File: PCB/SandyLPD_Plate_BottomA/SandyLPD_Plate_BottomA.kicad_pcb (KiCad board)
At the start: 2 copper layers, 131 x 83 mm, 14 parts

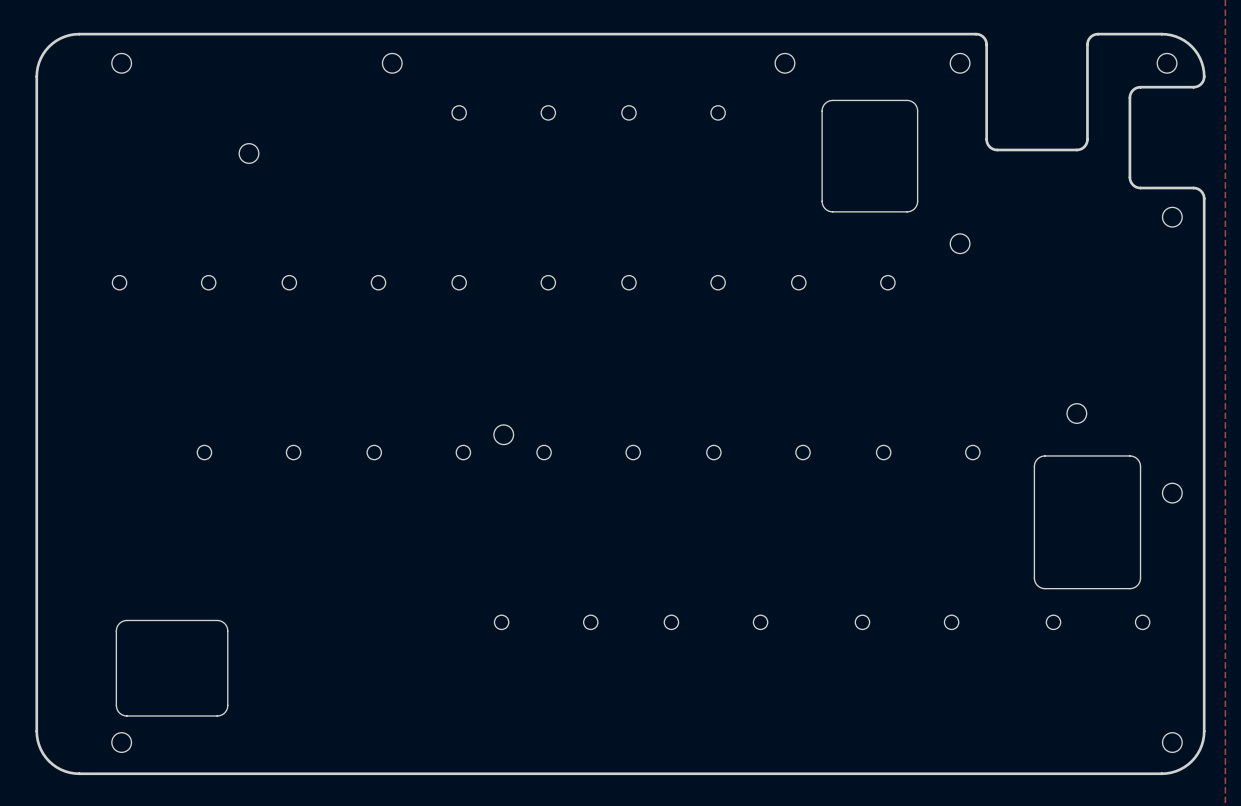
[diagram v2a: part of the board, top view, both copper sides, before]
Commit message: ネジ穴位置を再調整。
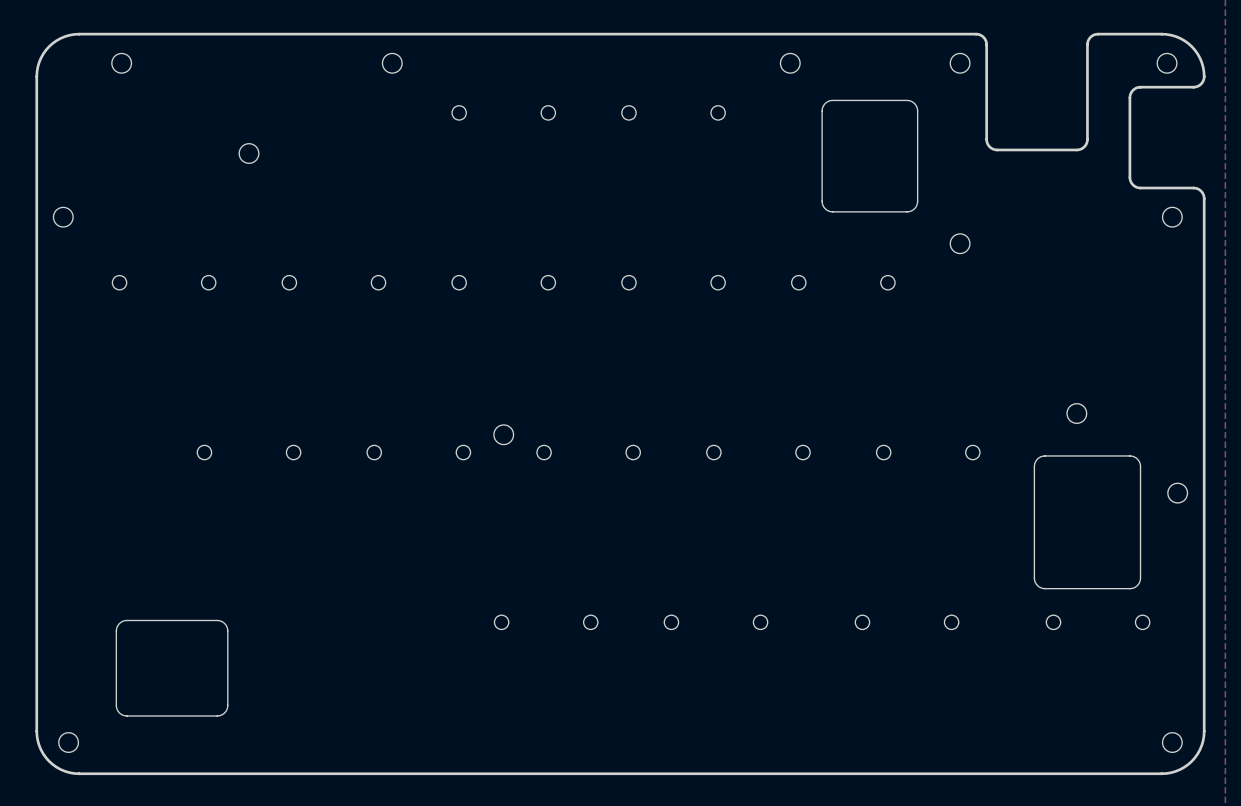
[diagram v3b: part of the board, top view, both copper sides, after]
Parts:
- added H_mid_8: MountingHole, locallib:MountingHole_2.2mm_M2_no_REF, F.Cu at (26.4, 52.6)
- moved H_btm_3 5.95 mm to (27.0, 111.5)
- moved H_mid_3 0.60 mm to (108.0, 35.3)
- moved H_mid_17 0.60 mm to (151.4, 83.6)
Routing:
- added copper zone on B.Cu, net (none)
- added copper zone on F.Cu, net (none)
- removed copper zone on B.Cu, net GND
- removed copper zone on F.Cu, net GND
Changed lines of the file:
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@@
 	)
 	(net 0 "")
-	(net 1 "GND")
 	(footprint "locallib:MountingHole_2.2mm_M2_no_REF"
 		(layer "F.Cu")
@@
 	(footprint "locallib:MountingHole_2.2mm_M2_no_REF"
 		(layer "F.Cu")
-		(at 150.836667 83.558138 180)
+		(at 151.431976 83.558138 180)
 		(descr "Mounting Hole 2.2mm, no annular, M2")
 		(tags "mounting hole 2.2mm no annular m2")
@@
 	(footprint "locallib:MountingHole_2.2mm_M2_no_REF"
 		(layer "F.Cu")
-		(at 107.378818 35.337425)
+		(at 107.974127 35.337425)
 		(descr "Mounting Hole 2.2mm, no annular, M2")
 		(tags "mounting hole 2.2mm no annular m2")
@@
 	(footprint "locallib:MountingHole_2.2mm_M2_no_REF"
 		(layer "F.Cu")
+		(at 26.416246 52.601856)
+		(descr "Mounting Hole 2.2mm, no annular, M2")
+		(tags "mounting hole 2.2mm no annular m2")
+		(property "Reference" "H_mid_8"
+			(at 0 -3.2 0)
+			(layer "F.SilkS")
+			(hide yes)
+			(effects
+				(font
+					(size 1 1)
+					(thickness 0.15)
+				)
+			)
+		)
+		(property "Value" "MountingHole"
+			(at 0 3.2 0)
+			(layer "F.Fab")
+			(effects
+				(font
+					(size 1 1)
+					(thickness 0.15)
+				)
+			)
+		)
+		(property "Footprint" "locallib:MountingHole_2.2mm_M2_no_REF"
+			(at 0 0 0)
+			(unlocked yes)
+			(layer "F.Fab")
+			(hide yes)
+			(effects
+				(font
+					(size 1.27 1.27)
+					(thickness 0.15)
+				)
+			)
+		)
+		(property "Datasheet" ""
+			(at 0 0 0)
+			(unlocked yes)
+			(layer "F.Fab")
+			(hide yes)
+			(effects
+				(font
+					(size 1.27 1.27)
+					(thickness 0.15)
+				)
+			)
+		)
+		(property "Description" "Mounting Hole without connection"
+			(at 0 0 0)
+			(unlocked yes)
+			(layer "F.Fab")
+			(hide yes)
+			(effects
+				(font
+					(size 1.27 1.27)
+					(thickness 0.15)
+				)
+			)
+		)
+		(property "LCSC-Reserve" ""
+			(at 0 0 0)
+			(unlocked yes)
+			(layer "F.Fab")
+			(hide yes)
+			(effects
+				(font
+					(size 1 1)
+					(thickness 0.15)
+				)
+			)
+		)
+		(property ki_fp_filters "MountingHole*")
+		(sheetname "ルート")
+		(sheetfile "SandyLPD_Plate_BottomA.kicad_sch")
+		(attr exclude_from_pos_files exclude_from_bom)
+		(fp_circle
+			(center 0 0)
+			(end 2.2 0)
+			(stroke
+				(width 0.15)
+				(type solid)
+			)
+			(fill none)
+			(layer "Cmts.User")
+		)
+		(fp_circle
+			(center 0 0)
+			(end 2.45 0)
+			(stroke
+				(width 0.05)
+				(type solid)
+			)
+			(fill none)
+			(layer "F.CrtYd")
+		)
+		(fp_text user "${REFERENCE}"
+			(at 0 0 0)
+			(layer "F.Fab")
+			(effects
+				(font
+					(size 1 1)
+					(thickness 0.15)
+				)
+			)
+		)
+		(pad "" np_thru_hole circle
+			(at 0 0)
+			(size 2.2 2.2)
+			(drill 2.2)
+			(layers "*.Cu" "*.Mask")
+		)
+	)
+	(footprint "locallib:MountingHole_2.2mm_M2_no_REF"
+		(layer "F.Cu")
 		(at 63.325656 35.337425)
 		(descr "Mounting Hole 2.2mm, no annular, M2")
@@
 	(footprint "locallib:MountingHole_2.2mm_M2_no_REF"
 		(layer "B.Cu")
-		(at 32.964693 111.537849 180)
+		(at 27.011559 111.537843 180)
 		(descr "Mounting Hole 2.2mm, no annular, M2")
 		(tags "mounting hole 2.2mm no annular m2")
@@
 	)
 	(zone
-		(net 1)
-		(net_name "GND")
+		(net 0)
+		(net_name "")
 		(layers "F&B.Cu")
 		(hatch edge 0.508)

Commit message: WIP　BaseにESDとヒューズ追加。ボトムAの穴位置調整中。
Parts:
- added C1: 10u, Capacitor_SMD:C_0805_2012Metric, B.Cu at (101.3, -48.5)
- added C10: 100n, Capacitor_SMD:C_0402_1005Metric, B.Cu at (129.4, -30.6)
- added C11: 100n, Capacitor_SMD:C_0402_1005Metric, B.Cu at (129.0, -34.8)
- added C12: 100n, Capacitor_SMD:C_0402_1005Metric, B.Cu at (125.8, -41.5)
- added C13: 2.2uF, Capacitor_SMD:C_0402_1005Metric, B.Cu at (125.8, -42.5)
- added C14: 2.2uF, Capacitor_SMD:C_0402_1005Metric, B.Cu at (121.6, -39.9)
- added C15: 2.2uF, Capacitor_SMD:C_0402_1005Metric, B.Cu at (120.6, -39.9)
- added C17: 10u, Capacitor_SMD:C_0805_2012Metric, B.Cu at (185.8, -48.3)
- added C18: 10u, Capacitor_SMD:C_0805_2012Metric, B.Cu at (185.8, -44.7)
- added C19: 100n, Capacitor_SMD:C_0402_1005Metric, B.Cu at (172.5, -22.9)
- added C2: 10u, Capacitor_SMD:C_0805_2012Metric, B.Cu at (101.3, -44.7)
- added C20: 100n, Capacitor_SMD:C_0402_1005Metric, B.Cu at (176.1, -37.6)
- added C21: 100n, Capacitor_SMD:C_0402_1005Metric, B.Cu at (181.3, -28.3)
- added C24: 100n, Capacitor_SMD:C_0402_1005Metric, B.Cu at (179.4, -32.5)
- added C28: 100n, Capacitor_SMD:C_0402_1005Metric, B.Cu at (173.5, -22.9)
- added C29: 100n, Capacitor_SMD:C_0402_1005Metric, B.Cu at (184.0, -41.1)
- added C3: 100n, Capacitor_SMD:C_0402_1005Metric, B.Cu at (125.7, -39.9)
- added C30: 100n, Capacitor_SMD:C_0402_1005Metric, B.Cu at (167.4, -28.4)
- added C31: 100n, Capacitor_SMD:C_0402_1005Metric, B.Cu at (175.1, -37.6)
- added C32: 100n, Capacitor_SMD:C_0402_1005Metric, B.Cu at (170.0, -37.6)
- added C33: 100n, Capacitor_SMD:C_0402_1005Metric, B.Cu at (168.4, -33.1)
- added C34: 2.2uF, Capacitor_SMD:C_0402_1005Metric, B.Cu at (185.2, -41.1)
- added C35: 2.2uF, Capacitor_SMD:C_0402_1005Metric, B.Cu at (172.0, -37.6)
- added C36: 2.2uF, Capacitor_SMD:C_0402_1005Metric, B.Cu at (171.0, -37.6)
- added C4: 100n, Capacitor_SMD:C_0402_1005Metric, B.Cu at (121.9, -25.4)
- added C5: 100n, Capacitor_SMD:C_0402_1005Metric, B.Cu at (124.7, -39.9)
- added C6: 100n, Capacitor_SMD:C_0402_1005Metric, B.Cu at (122.9, -25.4)
- added C7: 100n, Capacitor_SMD:C_0402_1005Metric, B.Cu at (118.0, -35.4)
- added C8: 100n, Capacitor_SMD:C_0402_1005Metric, B.Cu at (117.0, -30.3)
- added C9: 100n, Capacitor_SMD:C_0402_1005Metric, B.Cu at (119.6, -39.9)
- added D1: D, locallib:D_SOD-123_Emphasized_Direction_Line_Reference_on_bottom, B.Cu at (58.4, -48.2)
- added D10: D, locallib:D_SOD-123_Emphasized_Direction_Line_Reference_on_bottom, B.Cu at (67.9, -10.1)
- added D11: D, locallib:D_SOD-123_Emphasized_Direction_Line_Reference_on_bottom, B.Cu at (87.0, -10.1)
- added D12: D, locallib:D_SOD-123_Emphasized_Direction_Line_Reference_on_bottom, B.Cu at (106.0, -10.1)
- added D13: D, locallib:D_SOD-123_Emphasized_Direction_Line_Reference_on_bottom, B.Cu at (63.2, 8.95)
- added D14: D, locallib:D_SOD-123_Emphasized_Direction_Line_Reference_on_bottom, B.Cu at (82.2, 8.95)
- added D15: D, locallib:D_SOD-123_Emphasized_Direction_Line_Reference_on_bottom, B.Cu at (103.7, 8.95)
- added D16: D, locallib:D_SOD-123_Emphasized_Direction_Line_Reference_on_bottom, B.Cu at (125.1, 8.95)
- added D17: D, locallib:D_SOD-123_Emphasized_Direction_Line_Reference_on_bottom, B.Cu at (44.7, 14.3)
- added D18: D, locallib:D_SOD-123_Emphasized_Direction_Line_Reference_on_bottom, B.Cu at (206.1, -48.2)
- added D19: D, locallib:D_SOD-123_Emphasized_Direction_Line_Reference_on_bottom, B.Cu at (225.1, -48.2)
- added D2: D, locallib:D_SOD-123_Emphasized_Direction_Line_Reference_on_bottom, B.Cu at (77.5, -48.2)
- added D20: D, locallib:D_SOD-123_Emphasized_Direction_Line_Reference_on_bottom, B.Cu at (187.0, -29.1)
- added D21: D, locallib:D_SOD-123_Emphasized_Direction_Line_Reference_on_bottom, B.Cu at (206.1, -29.1)
- added D22: D, locallib:D_SOD-123_Emphasized_Direction_Line_Reference_on_bottom, B.Cu at (225.1, -29.1)
- added D23: D, locallib:D_SOD-123_Emphasized_Direction_Line_Reference_on_bottom, B.Cu at (244.2, -29.1)
- added D24: D, locallib:D_SOD-123_Emphasized_Direction_Line_Reference_on_bottom, B.Cu at (263.2, -29.1)
- added D25: D, locallib:D_SOD-123_Emphasized_Direction_Line_Reference_on_bottom, B.Cu at (177.5, -10.1)
- added D26: D, locallib:D_SOD-123_Emphasized_Direction_Line_Reference_on_bottom, B.Cu at (196.5, -10.1)
- added D27: D, locallib:D_SOD-123_Emphasized_Direction_Line_Reference_on_bottom, B.Cu at (215.6, -10.1)
- added D28: D, locallib:D_SOD-123_Emphasized_Direction_Line_Reference_on_bottom, B.Cu at (234.6, -10.1)
- added D29: D, locallib:D_SOD-123_Emphasized_Direction_Line_Reference_on_bottom, B.Cu at (253.7, -10.1)
- added D3: D, locallib:D_SOD-123_Emphasized_Direction_Line_Reference_on_bottom, B.Cu at (20.3, -29.1)
- added D30: D, locallib:D_SOD-123_Emphasized_Direction_Line_Reference_on_bottom, B.Cu at (158.4, 8.95)
- added D31: D, locallib:D_SOD-123_Emphasized_Direction_Line_Reference_on_bottom, B.Cu at (179.9, 8.95)
- added D32: D, locallib:D_SOD-123_Emphasized_Direction_Line_Reference_on_bottom, B.Cu at (201.3, 8.95)
- added D33: D, locallib:D_SOD-123_Emphasized_Direction_Line_Reference_on_bottom, B.Cu at (220.3, 8.95)
- added D34: D, locallib:D_SOD-123_Emphasized_Direction_Line_Reference_on_bottom, B.Cu at (240.0, 14.3)
- added D35: D, locallib:D_SOD-123_Emphasized_Direction_Line_Reference_on_bottom, B.Cu at (32.2, 8.95)
- added D4: D, locallib:D_SOD-123_Emphasized_Direction_Line_Reference_on_bottom, B.Cu at (39.4, -29.1)
- added D45: D, locallib:D_SOD-123_Emphasized_Direction_Line_Reference_on_bottom, B.Cu at (263.2, 8.95)
- added D5: D, locallib:D_SOD-123_Emphasized_Direction_Line_Reference_on_bottom, B.Cu at (58.4, -29.1)
- added D6: D, locallib:D_SOD-123_Emphasized_Direction_Line_Reference_on_bottom, B.Cu at (77.5, -29.1)
- added D7: D, locallib:D_SOD-123_Emphasized_Direction_Line_Reference_on_bottom, B.Cu at (96.5, -29.1)
- added D8: D, locallib:D_SOD-123_Emphasized_Direction_Line_Reference_on_bottom, B.Cu at (29.8, -10.1)
- added D9: D, locallib:D_SOD-123_Emphasized_Direction_Line_Reference_on_bottom, B.Cu at (48.9, -10.1)
- added D96: PRTR5V0U2X, Package_TO_SOT_SMD:SOT-143, B.Cu at (132.3, -47.5)
- added D97: PRTR5V0U2X, Package_TO_SOT_SMD:SOT-143, B.Cu at (163.2, -47.4)
- added D98: PRTR5V0U2X, Package_TO_SOT_SMD:SOT-143, B.Cu at (123.4, -51.2)
- added D99: PRTR5V0U2X, Package_TO_SOT_SMD:SOT-143, B.Cu at (172.0, -51.2)
- added F1: Fuse, Fuse:Fuse_1206_3216Metric, B.Cu at (115.9, -53.3)
- added F2: Fuse, Fuse:Fuse_1206_3216Metric, B.Cu at (179.7, -54.3)
- added F3: Fuse, Fuse:Fuse_1206_3216Metric, B.Cu at (131.7, -51.6)
- added F4: Fuse, Fuse:Fuse_1206_3216Metric, B.Cu at (163.7, -51.6)
- added G***: LOGO, locallib:ICON_USB, F.Cu at (124.1, -58.3)
- added G***: LOGO, locallib:ICON_USB, F.Cu at (171.3, -58.3)
- added H_btm_1: MountingHole, locallib:MountingHole_M2_Through-hole_tap_THC-0.8-1.0-2_minimal, B.Cu at (64.4, -17.2)
- added H_btm_2: MountingHole, locallib:MountingHole_M2_Through-hole_tap_THC-0.8-1.0-2_minimal, B.Cu at (15.6, 17.3)
- added H_btm_3: MountingHole, locallib:MountingHole_M2_Through-hole_tap_THC-0.8-1.0-2_minimal, B.Cu at (139.4, 17.3)
- added H_btm_4: MountingHole, locallib:MountingHole_M2_Through-hole_tap_THC-0.8-1.0-2_minimal, B.Cu at (231.1, -17.2)
- added H_btm_5: MountingHole, locallib:MountingHole_M2_Through-hole_tap_THC-0.8-1.0-2_minimal, B.Cu at (156.0, 17.3)
- added H_btm_6: MountingHole, locallib:MountingHole_M2_Through-hole_tap_THC-0.8-1.0-2_minimal, B.Cu at (279.9, 17.3)
- added H_mid_1: MountingHole, locallib:MountingHole_M2_Through-hole_tap_THC-0.8-2.0-2_minimal, F.Cu at (21.5, -58.9)
- added H_mid_10: MountingHole, locallib:MountingHole_M2_Through-hole_tap_THC-0.8-2.0-2_minimal, F.Cu at (128.7, -19.6)
- added H_mid_11: MountingHole, locallib:MountingHole_M2_Through-hole_tap_THC-0.8-2.0-2_minimal, F.Cu at (140.0, -10.7)
- added H_mid_12: MountingHole, locallib:MountingHole_M2_Through-hole_tap_THC-0.8-2.0-2_minimal, F.Cu at (156.6, -58.9)
- added H_mid_13: MountingHole, locallib:MountingHole_M2_Through-hole_tap_THC-0.8-2.0-2_minimal, F.Cu at (179.9, -58.9)
- added H_mid_14: MountingHole, locallib:MountingHole_M2_Through-hole_tap_THC-0.8-2.0-2_minimal, F.Cu at (198.9, -58.9)
- added H_mid_15: MountingHole, locallib:MountingHole_M2_Through-hole_tap_THC-0.8-2.0-2_minimal, F.Cu at (243.6, -58.9)
- added H_mid_16: MountingHole, locallib:MountingHole_M2_Through-hole_tap_THC-0.8-2.0-2_minimal, F.Cu at (273.9, -58.9)
- added H_mid_17: MountingHole, locallib:MountingHole_M2_Through-hole_tap_THC-0.8-2.0-2_minimal, F.Cu at (156.0, -41.6)
- added H_mid_18: MountingHole, locallib:MountingHole_M2_Through-hole_tap_THC-0.8-2.0-2_minimal, F.Cu at (179.9, -38.7)
- added H_mid_19: MountingHole, locallib:MountingHole_M2_Through-hole_tap_THC-0.8-2.0-2_minimal, F.Cu at (259.6, -48.8)
- added H_mid_2: MountingHole, locallib:MountingHole_M2_Through-hole_tap_THC-0.8-2.0-2_minimal, F.Cu at (51.9, -58.9)
- added H_mid_20: MountingHole, locallib:MountingHole_M2_Through-hole_tap_THC-0.8-2.0-2_minimal, F.Cu at (280.5, -41.6)
- added H_mid_21: MountingHole, locallib:MountingHole_M2_Through-hole_tap_THC-0.8-2.0-2_minimal, F.Cu at (166.8, -19.6)
- added H_mid_22: MountingHole, locallib:MountingHole_M2_Through-hole_tap_THC-0.8-2.0-2_minimal, F.Cu at (155.5, -10.7)
- added H_mid_3: MountingHole, locallib:MountingHole_M2_Through-hole_tap_THC-0.8-2.0-2_minimal, F.Cu at (96.5, -58.9)
- added H_mid_4: MountingHole, locallib:MountingHole_M2_Through-hole_tap_THC-0.8-2.0-2_minimal, F.Cu at (115.6, -58.9)
- added H_mid_5: MountingHole, locallib:MountingHole_M2_Through-hole_tap_THC-0.8-2.0-2_minimal, F.Cu at (138.8, -58.9)
- added H_mid_6: MountingHole, locallib:MountingHole_M2_Through-hole_tap_THC-0.8-2.0-2_minimal, F.Cu at (15.0, -41.6)
- added H_mid_7: MountingHole, locallib:MountingHole_M2_Through-hole_tap_THC-0.8-2.0-2_minimal, F.Cu at (35.8, -48.8)
- added H_mid_8: MountingHole, locallib:MountingHole_M2_Through-hole_tap_THC-0.8-2.0-2_minimal, F.Cu at (115.6, -38.7)
- added H_mid_9: MountingHole, locallib:MountingHole_M2_Through-hole_tap_THC-0.8-2.0-2_minimal, F.Cu at (139.4, -41.6)
- added J1: Conn_02x02_Odd_Even, locallib:PinHeader_2x02_P2.00mm_Vertical_2pair, B.Cu at (135.2, -17.8)
- added J10: Conn_01x10_Pin, Connector_PinHeader_1.00mm:PinHeader_1x10_P1.00mm_Vertical, B.Cu at (158.2, -24.3)
- added J11: Conn_01x03, locallib:PinHeader_1x03_P2.54mm_Vertical_All_circle, B.Cu at (171.5, -17.4)
- added J2: Conn_01x03, locallib:PinHeader_1x03_P2.54mm_Vertical_All_circle, B.Cu at (123.9, -17.4)
- added J4: Conn_01x10_Pin, Connector_PinHeader_1.00mm:PinHeader_1x10_P1.00mm_Vertical, B.Cu at (137.0, -30.5)
- added J5: USB_C_Receptacle_USB2.0, locallib:USB_C_Receptacle_HRO_TYPE-C-31-M-12, B.Cu at (123.9, -58.6)
- added J6: USB_C_Receptacle_USB2.0, locallib:USB_C_Receptacle_HRO_TYPE-C-31-M-12, B.Cu at (139.4, -50.6)
- added J7: USB_C_Receptacle_USB2.0, locallib:USB_C_Receptacle_HRO_TYPE-C-31-M-12, B.Cu at (156.1, -50.6)
- added J8: USB_C_Receptacle_USB2.0, locallib:USB_C_Receptacle_HRO_TYPE-C-31-M-12, B.Cu at (171.5, -58.6)
- added J9: Conn_02x02_Odd_Even, locallib:PinHeader_2x02_P2.00mm_Vertical_2pair, B.Cu at (160.2, -15.9)
- added JP1: SolderJumper_2_Open, locallib:SolderJumper-2_P1.3mm_Open_RoundedPad1.0x1.5mm_no_Courtyard, B.Cu at (130.7, -8.72)
- added JP3: SolderJumper_2_Open, locallib:SolderJumper-2_P1.3mm_Open_RoundedPad1.0x1.5mm_no_Courtyard, B.Cu at (164.5, -8.77)
- added L1: WS2812B-2020, locallib:LED_WS2812B-2020_PLCC4_2.0x2.0mm_with_3D_model, F.Cu at (21.5, -14.9)
- added L2: WS2812B-2020, locallib:LED_WS2812B-2020_PLCC4_2.0x2.0mm_with_3D_model, F.Cu at (21.5, -10.1)
- added L3: WS2812B-2020, locallib:LED_WS2812B-2020_PLCC4_2.0x2.0mm_with_3D_model, F.Cu at (21.5, -5.33)
- added L4: WS2812B-2020, locallib:LED_WS2812B-2020_PLCC4_2.0x2.0mm_with_3D_model, F.Cu at (273.9, -14.9)
- added L5: WS2812B-2020, locallib:LED_WS2812B-2020_PLCC4_2.0x2.0mm_with_3D_model, F.Cu at (273.9, -10.1)
- added L6: WS2812B-2020, locallib:LED_WS2812B-2020_PLCC4_2.0x2.0mm_with_3D_model, F.Cu at (273.9, -5.33)
- added LS1: Speaker, Buzzer_Beeper:Buzzer_Murata_PKMCS0909E, B.Cu at (26.3, 8.95)
- added LS2: Speaker, Buzzer_Beeper:Buzzer_Murata_PKMCS0909E, B.Cu at (269.2, 8.95)
- added Q1: AO3401A, Package_TO_SOT_SMD:SOT-23, B.Cu at (107.0, -52.4)
- added Q2: DMMT5401, Package_TO_SOT_SMD:SC-74-6_1.55x2.9mm_P0.95mm, B.Cu at (103.1, -52.5)
- added Q3: AO3401A, Package_TO_SOT_SMD:SOT-23, B.Cu at (192.3, -52.2)
- added Q4: DMMT5401, Package_TO_SOT_SMD:SC-74-6_1.55x2.9mm_P0.95mm, B.Cu at (188.2, -52.2)
- added R1: 1k, Resistor_SMD:R_0402_1005Metric, B.Cu at (125.1, -6.07)
- added R10: 5.1k, Resistor_SMD:R_0402_1005Metric, B.Cu at (120.3, -52.4)
- added R11: 5.1k, Resistor_SMD:R_0402_1005Metric, B.Cu at (126.3, -52.4)
- added R12: 5.6k, Resistor_SMD:R_0402_1005Metric, B.Cu at (112.9, -52.7)
- added R13: 5.1k, Resistor_SMD:R_0402_1005Metric, B.Cu at (169.0, -52.4)
- added R14: 1k, Resistor_SMD:R_0402_1005Metric, B.Cu at (263.2, 5.38)
- added R15: 5.1k, Resistor_SMD:R_0402_1005Metric, B.Cu at (175.0, -52.4)
- added R16: 5.6k, Resistor_SMD:R_0402_1005Metric, B.Cu at (183.5, -54.1)
- added R17: 27, Resistor_SMD:R_0402_1005Metric, B.Cu at (174.0, -37.6)
- added R18: 27, Resistor_SMD:R_0402_1005Metric, B.Cu at (173.0, -37.6)
- added R19: 10k, Resistor_SMD:R_0402_1005Metric, B.Cu at (183.5, -51.5)
- added R2: 27, Resistor_SMD:R_0402_1005Metric, B.Cu at (123.6, -39.9)
- added R20: 10k, Resistor_SMD:R_0402_1005Metric, B.Cu at (187.0, -40.7)
- added R21: 1k, Resistor_SMD:R_0402_1005Metric, B.Cu at (189.2, -40.7)
- added R22: 1k, Resistor_SMD:R_0402_1005Metric, B.Cu at (174.5, -22.9)
- added R23: 10k, Resistor_SMD:R_0402_1005Metric, B.Cu at (100.3, -53.3)
- added R24: 10k, Resistor_SMD:R_0402_1005Metric, B.Cu at (100.3, -51.3)
- added R25: 10k, Resistor_SMD:R_0402_1005Metric, B.Cu at (185.3, -53.0)
- added R26: 10k, Resistor_SMD:R_0402_1005Metric, B.Cu at (185.3, -51.0)
- added R3: 27, Resistor_SMD:R_0402_1005Metric, B.Cu at (122.6, -39.9)
- added R4: 10k, Resistor_SMD:R_0402_1005Metric, B.Cu at (130.0, -42.5)
- added R5: 1k, Resistor_SMD:R_0402_1005Metric, B.Cu at (132.2, -42.5)
- added R6: 1k, Resistor_SMD:R_0402_1005Metric, B.Cu at (123.9, -25.4)
- added R7: 1k, Resistor_SMD:R_0402_1005Metric, B.Cu at (170.3, -5.72)
- added R8: 10k, Resistor_SMD:R_0402_1005Metric, B.Cu at (112.9, -50.0)
- added R9: 1k, Resistor_SMD:R_0402_1005Metric, B.Cu at (32.2, 5.38)
- added REF**: ICON_Through-hole_Tap_Long, locallib:ICON_Through-hole_Tap_Long, F.Cu at (198.9, -54.1)
- added REF**: ICON_Through-hole_Tap_Long, locallib:ICON_Through-hole_Tap_Long, F.Cu at (133.9, -57.0)
- added REF**: ICON_Through-hole_Tap_Long, locallib:ICON_Through-hole_Tap_Long, F.Cu at (21.5, -54.1)
- added REF**: ICON_Through-hole_Tap_Long, locallib:ICON_Through-hole_Tap_Long, F.Cu at (158.4, -7.12)
- added REF**: 60_Outline, locallib:SandyLP-Duo_outline_Base, F.Cu at (147.7, -10.1)
- added REF**: ICON_Through-hole_Tap_Long, locallib:ICON_Through-hole_Tap_Long, F.Cu at (243.6, -54.1)
- added REF**: ICON_Through-hole_Tap_Long, locallib:ICON_Through-hole_Tap_Long, F.Cu at (166.8, -14.9)
- added REF**: ICON_Through-hole_Tap_Long, locallib:ICON_Through-hole_Tap_Long, F.Cu at (276.9, -38.1)
- added REF**: ICON_Through-hole_Tap_Long, locallib:ICON_Through-hole_Tap_Long, F.Cu at (160.8, -57.1)
- added REF**: ICON_Through-hole_Tap_Long, locallib:ICON_Through-hole_Tap_Long, F.Cu at (136.4, -7.12)
- added REF**: ICON_Through-hole_Tap_Long, locallib:ICON_Through-hole_Tap_Long, F.Cu at (51.9, -54.1)
- added REF**: ICON_Through-hole_Tap_Long, locallib:ICON_Through-hole_Tap_Long, F.Cu at (128.7, -14.9)
- added REF**: ICON_Through-hole_Tap_Long, locallib:ICON_Through-hole_Tap_Long, F.Cu at (179.9, -33.9)
- added REF**: ICON_Through-hole_Tap_Long, locallib:ICON_Through-hole_Tap_Long, F.Cu at (18.1, -45.3)
- added REF**: ICON_Through-hole_Tap_Long, locallib:ICON_Through-hole_Tap_Long, F.Cu at (158.4, -38.1)
- added REF**: ICON_Through-hole_Tap_Long, locallib:ICON_Through-hole_Tap_Long, F.Cu at (273.9, -54.1)
- added REF**: ICON_Through-hole_Tap, locallib:ICON_Through-hole_Tap, B.Cu at (160.2, 17.9)
- added REF**: ICON_Through-hole_Tap, locallib:ICON_Through-hole_Tap, B.Cu at (275.1, 17.3)
- added REF**: ICON_Through-hole_Tap, locallib:ICON_Through-hole_Tap, B.Cu at (68.5, -16.6)
- added REF**: ICON_Through-hole_Tap, locallib:ICON_Through-hole_Tap, B.Cu at (135.2, 18.5)
- added REF**: ICON_Through-hole_Tap, locallib:ICON_Through-hole_Tap, B.Cu at (226.3, -17.8)
- added REF**: ICON_Through-hole_Tap_Long, locallib:ICON_Through-hole_Tap_Long, F.Cu at (113.8, -54.1)
- added REF**: ICON_Through-hole_Tap, locallib:ICON_Through-hole_Tap, B.Cu at (19.7, 17.3)
- added REF**: ICON_Through-hole_Tap_Long, locallib:ICON_Through-hole_Tap_Long, F.Cu at (96.5, -54.1)
- added REF**: ICON_Through-hole_Tap_Long, locallib:ICON_Through-hole_Tap_Long, F.Cu at (115.6, -33.9)
- added REF**: ICON_Through-hole_Tap_Long, locallib:ICON_Through-hole_Tap_Long, F.Cu at (181.6, -54.7)
- added REF**: ICON_Through-hole_Tap_Long, locallib:ICON_Through-hole_Tap_Long, F.Cu at (264.4, -48.2)
- added REF**: ICON_Through-hole_Tap_Long, locallib:ICON_Through-hole_Tap_Long, F.Cu at (31.0, -48.2)
- added REF**: ICON_Through-hole_Tap_Long, locallib:ICON_Through-hole_Tap_Long, F.Cu at (136.4, -37.5)
- added STLED1: LED_GREEN, LED_SMD:LED_0805_2012Metric, B.Cu at (125.1, -2.95)
- added STLED2: LED_GREEN, LED_SMD:LED_0805_2012Metric, B.Cu at (170.3, -2.95)
- added SW1: BOOT_ALT, Button_Switch_SMD:SW_SPST_PTS810, B.Cu at (132.8, -3.55)
- added SW2: RESET_ALT, Button_Switch_SMD:SW_SPST_PTS810, B.Cu at (128.7, -3.55)
- added SW3: SW_DIP_x04, Button_Switch_SMD:SW_DIP_SPSTx04_Slide_Copal_CHS-04B_W7.62mm_P1.27mm, B.Cu at (131.0, -10.7)
- added SW4: BOOT_ALT, Button_Switch_SMD:SW_SPST_PTS810, B.Cu at (162.7, -3.55)
- added SW5: RESET_ALT, Button_Switch_SMD:SW_SPST_PTS810, B.Cu at (166.9, -3.55)
- added SW6: SW_DIP_x04, Button_Switch_SMD:SW_DIP_SPSTx04_Slide_Copal_CHS-04B_W7.62mm_P1.27mm, B.Cu at (164.4, -10.7)
- added SW_1: W, locallib:Kailh_socket_ChocV2, F.Cu at (64.4, -48.2)
- added SW_10: C, locallib:Kailh_socket_ChocV2, F.Cu at (73.9, -10.1)
- added SW_11: V, locallib:Kailh_socket_ChocV2, F.Cu at (92.9, -10.1)
- added SW_12: B, locallib:Kailh_socket_ChocV2, F.Cu at (112.0, -10.1)
- added SW_13: L_RE, locallib:ChocV2_AND_RotaryEncoder_Alps_EC11E-Switch_Vertical_H20mm_NPTH_MP_minimal, F.Cu at (50.1, 8.95)
- added SW_14: LALT, locallib:Kailh_socket_ChocV2, F.Cu at (88.2, 8.96)
- added SW_15: LSPC, locallib:Kailh_socket_ChocV2, F.Cu at (109.6, 8.95)
- added SW_16: L_CNT, locallib:Kailh_socket_ChocV2, F.Cu at (131.0, 8.96)
- added SW_17: I, locallib:Kailh_socket_ChocV2, F.Cu at (212.0, -48.2)
- added SW_18: O, locallib:Kailh_socket_ChocV2, F.Cu at (231.1, -48.2)
- added SW_19: J, locallib:Kailh_socket_ChocV2, F.Cu at (193.0, -29.1)
- added SW_2: E, locallib:Kailh_socket_ChocV2, F.Cu at (83.4, -48.2)
- added SW_20: K, locallib:Kailh_socket_ChocV2, F.Cu at (212.0, -29.1)
- added SW_21: L, locallib:Kailh_socket_ChocV2, F.Cu at (231.1, -29.1)
- added SW_22: -, locallib:Kailh_socket_ChocV2, F.Cu at (250.1, -29.1)
- added SW_23: ENT, locallib:Kailh_socket_ChocV2, F.Cu at (269.2, -29.1)
- added SW_24: N, locallib:Kailh_socket_ChocV2, F.Cu at (183.4, -10.1)
- added SW_25: M, locallib:Kailh_socket_ChocV2, F.Cu at (202.5, -10.1)
- added SW_26: <,, locallib:Kailh_socket_ChocV2, F.Cu at (221.5, -10.1)
- added SW_27: >., locallib:Kailh_socket_ChocV2, F.Cu at (240.6, -10.1)
- added SW_28: ?/, locallib:Kailh_socket_ChocV2, F.Cu at (259.6, -10.1)
- added SW_29: R_RE, locallib:ChocV2_AND_RotaryEncoder_Alps_EC11E-Switch_Vertical_H20mm_NPTH_MP_minimal, F.Cu at (245.3, 8.95)
- added SW_3: LCTL, locallib:Kailh_socket_ChocV2, F.Cu at (26.3, -29.1)
- added SW_30: R_CNT, locallib:Kailh_socket_ChocV2, F.Cu at (164.4, 8.96)
- added SW_31: RSPC, locallib:Kailh_socket_ChocV2, F.Cu at (185.8, 8.95)
- added SW_32: RALT, locallib:Kailh_socket_ChocV2, F.Cu at (207.2, 8.96)
- added SW_33: RWIN, locallib:Kailh_socket_ChocV2, F.Cu at (226.3, 8.95)
- added SW_4: A, locallib:Kailh_socket_ChocV2, F.Cu at (45.3, -29.1)
- added SW_5: S, locallib:Kailh_socket_ChocV2, F.Cu at (64.4, -29.1)
- added SW_6: D, locallib:Kailh_socket_ChocV2, F.Cu at (83.4, -29.1)
- added SW_7: F, locallib:Kailh_socket_ChocV2, F.Cu at (102.5, -29.1)
- added SW_8: Z, locallib:Kailh_socket_ChocV2, F.Cu at (35.8, -10.1)
- added SW_9: X, locallib:Kailh_socket_ChocV2, F.Cu at (54.8, -10.1)
- added SW_LWIN1: LWIN, locallib:Kailh_socket_ChocV2, F.Cu at (69.1, 8.96)
- added T_L_C0: Conn_01x01, locallib:TestPoint_THTPad_D2.0mm_Drill1.0mm, B.Cu at (38.8, -0.57)
- added T_L_C1: Conn_01x01, locallib:TestPoint_THTPad_D2.0mm_Drill1.0mm, B.Cu at (59.6, 6.57)
- added T_L_C2: Conn_01x01, locallib:TestPoint_THTPad_D2.0mm_Drill1.0mm, B.Cu at (78.7, 16.1)
- added T_L_C3: Conn_01x01, locallib:TestPoint_THTPad_D2.0mm_Drill1.0mm, B.Cu at (97.7, 16.1)
- added T_L_C4: Conn_01x01, locallib:TestPoint_THTPad_D2.0mm_Drill1.0mm, B.Cu at (119.1, 16.1)
- added T_L_C5: Conn_01x01, locallib:TestPoint_THTPad_D2.0mm_Drill1.0mm, B.Cu at (140.6, 11.9)
- added T_L_R0: Conn_01x01, locallib:TestPoint_THTPad_D2.0mm_Drill1.0mm, B.Cu at (49.5, -50.6)
- added T_L_R1: Conn_01x01, locallib:TestPoint_THTPad_D2.0mm_Drill1.0mm, B.Cu at (16.1, -30.3)
- added T_L_R2: Conn_01x01, locallib:TestPoint_THTPad_D2.0mm_Drill1.0mm, B.Cu at (44.1, -11.9)
- added T_L_R3: Conn_01x01, locallib:TestPoint_THTPad_D2.0mm_Drill1.0mm, B.Cu at (40.6, 13.1)
- added T_R_C0: Conn_01x01, locallib:TestPoint_THTPad_D2.0mm_Drill1.0mm, B.Cu at (266.2, -4.14)
- added T_R_C1: Conn_01x01, locallib:TestPoint_THTPad_D2.0mm_Drill1.0mm, B.Cu at (254.9, 4.19)
- added T_R_C2: Conn_01x01, locallib:TestPoint_THTPad_D2.0mm_Drill1.0mm, B.Cu at (235.8, 16.1)
- added T_R_C3: Conn_01x01, locallib:TestPoint_THTPad_D2.0mm_Drill1.0mm, B.Cu at (217.2, 16.1)
- added T_R_C4: Conn_01x01, locallib:TestPoint_THTPad_D2.0mm_Drill1.0mm, B.Cu at (195.3, 16.1)
- added T_R_C5: Conn_01x01, locallib:TestPoint_THTPad_D2.0mm_Drill1.0mm, B.Cu at (173.9, 16.1)
- added T_R_R0: Conn_01x01, locallib:TestPoint_THTPad_D2.0mm_Drill1.0mm, B.Cu at (184.6, -57.3)
- added T_R_R1: Conn_01x01, locallib:TestPoint_THTPad_D2.0mm_Drill1.0mm, B.Cu at (278.7, -31.5)
- added T_R_R2: Conn_01x01, locallib:TestPoint_THTPad_D2.0mm_Drill1.0mm, B.Cu at (266.2, -10.1)
- added T_R_R3: Conn_01x01, locallib:TestPoint_THTPad_D2.0mm_Drill1.0mm, B.Cu at (216.8, 5.98)
- added U1: NCP1117-3.3_SOT223, Package_TO_SOT_SMD:SOT-223-3_TabPin2, B.Cu at (106.8, -46.7)
- added U2: NCP1117-3.3_SOT223, Package_TO_SOT_SMD:SOT-223-3_TabPin2, B.Cu at (191.4, -46.5)
- added U3: RP2040, locallib:RP2040-QFN-56, B.Cu at (123.5, -31.9)
- added U4: W25Q128JVPIQ, Package_SON:WSON-8-1EP_6x5mm_P1.27mm_EP3.4x4.3mm, B.Cu at (130.2, -39.1)
- added U5: RP2040, locallib:RP2040-QFN-56, B.Cu at (173.9, -29.7)
- added U6: W25Q128JVPIQ, Package_SON:WSON-8-1EP_6x5mm_P1.27mm_EP3.4x4.3mm, B.Cu at (187.2, -37.3)
- added Y1: 12MHz, Crystal:Resonator_SMD_Murata_CSTxExxV-3Pin_3.0x1.1mm, B.Cu at (123.9, -22.9)
- added Y2: 12MHz, Crystal:Resonator_SMD_Murata_CSTxExxV-3Pin_3.0x1.1mm, B.Cu at (174.5, -20.5)
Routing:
- net (no net): track 0.00 -> 5727.2 mm, vias 0 -> 242
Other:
- board size 131 x 83 mm -> 271.5 x 101 mm
- board text added: "#SandyLP_Duo DN0010 by @jpskenn"
- board text added: "1 2 3 4"
- board text added: "BOOT"
- board text added: "L Back"
- board text added: "Legitimate Anger"
- board text added: "R Back"
- board text added: "RESET"
- board text added: "Through-hole tap head diameter"
- board text added: "⌨️"

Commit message: 穴位置調整。ざっくりOK。
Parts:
- removed C1, C17, C18, C2: 10u, Capacitor_SMD:C_0805_2012Metric
- removed C10, C11, C12, C19, C20, C21, C24, C28, C29, C3, C30, C31, C32, C33, C4, C5, C6, C7, C8, C9: 100n, Capacitor_SMD:C_0402_1005Metric
- removed C13, C14, C15, C34, C35, C36: 2.2uF, Capacitor_SMD:C_0402_1005Metric
- removed D1, D10, D11, D12, D13, D14, D15, D16, D17, D18, D19, D2, D20, D21, D22, D23, D24, D25, D26, D27, D28, D29, D3, D30, D31, D32, D33, D34, D35, D4, D45, D5, D6, D7, D8, D9: D, locallib:D_SOD-123_Emphasized_Direction_Line_Reference_on_bottom
- removed D96, D97, D98, D99: PRTR5V0U2X, Package_TO_SOT_SMD:SOT-143
- removed F1, F2, F3, F4: Fuse, Fuse:Fuse_1206_3216Metric
- removed G*** (x2): LOGO, locallib:ICON_USB
- removed the H_btm_1 at (64.4, -17.2)
- removed H_btm_2, H_btm_5, H_btm_6: MountingHole, locallib:MountingHole_M2_Through-hole_tap_THC-0.8-1.0-2_minimal
- removed the H_btm_3 at (139.4, 17.3)
- removed the H_btm_4 at (231.1, -17.2)
- removed the H_mid_1 at (21.5, -58.9)
- removed the H_mid_10 at (128.7, -19.6)
- removed H_mid_11, H_mid_12, H_mid_13, H_mid_14, H_mid_16, H_mid_18, H_mid_22, H_mid_4, H_mid_5, H_mid_6, H_mid_7: MountingHole, locallib:MountingHole_M2_Through-hole_tap_THC-0.8-2.0-2_minimal
- removed the H_mid_15 at (243.6, -58.9)
- removed the H_mid_17 at (156.0, -41.6)
- removed the H_mid_19 at (259.6, -48.8)
- removed the H_mid_2 at (51.9, -58.9)
- removed the H_mid_20 at (280.5, -41.6)
- removed the H_mid_21 at (166.8, -19.6)
- removed the H_mid_3 at (96.5, -58.9)
- removed the H_mid_8 at (115.6, -38.7)
- removed the H_mid_9 at (139.4, -41.6)
- removed J1, J9: Conn_02x02_Odd_Even, locallib:PinHeader_2x02_P2.00mm_Vertical_2pair
- removed J10, J4: Conn_01x10_Pin, Connector_PinHeader_1.00mm:PinHeader_1x10_P1.00mm_Vertical
- removed J11, J2: Conn_01x03, locallib:PinHeader_1x03_P2.54mm_Vertical_All_circle
- removed J5, J6, J7, J8: USB_C_Receptacle_USB2.0, locallib:USB_C_Receptacle_HRO_TYPE-C-31-M-12
- removed JP1, JP3: SolderJumper_2_Open, locallib:SolderJumper-2_P1.3mm_Open_RoundedPad1.0x1.5mm_no_Courtyard
- removed L1, L2, L3, L4, L5, L6: WS2812B-2020, locallib:LED_WS2812B-2020_PLCC4_2.0x2.0mm_with_3D_model
- removed LS1, LS2: Speaker, Buzzer_Beeper:Buzzer_Murata_PKMCS0909E
- removed Q1, Q3: AO3401A, Package_TO_SOT_SMD:SOT-23
- removed Q2, Q4: DMMT5401, Package_TO_SOT_SMD:SC-74-6_1.55x2.9mm_P0.95mm
- removed R1, R14, R21, R22, R5, R6, R7, R9: 1k, Resistor_SMD:R_0402_1005Metric
- removed R10, R11, R13, R15: 5.1k, Resistor_SMD:R_0402_1005Metric
- removed R12, R16: 5.6k, Resistor_SMD:R_0402_1005Metric
- removed R17, R18, R2, R3: 27, Resistor_SMD:R_0402_1005Metric
- removed R19, R20, R23, R24, R25, R26, R4, R8: 10k, Resistor_SMD:R_0402_1005Metric
- removed the REF** at (198.9, -54.1)
- removed the REF** at (133.9, -57.0)
- removed the REF** at (21.5, -54.1)
- removed the REF** at (158.4, -7.12)
- removed the REF** at (147.7, -10.1)
- removed the REF** at (243.6, -54.1)
- removed the REF** at (166.8, -14.9)
- removed the REF** at (276.9, -38.1)
- removed the REF** at (160.8, -57.1)
- removed the REF** at (136.4, -7.12)
- removed the REF** at (51.9, -54.1)
- removed the REF** at (128.7, -14.9)
- removed the REF** at (179.9, -33.9)
- removed the REF** at (18.1, -45.3)
- removed the REF** at (158.4, -38.1)
- removed the REF** at (273.9, -54.1)
- removed the REF** at (160.2, 17.9)
- removed the REF** at (275.1, 17.3)
- removed the REF** at (68.5, -16.6)
- removed the REF** at (135.2, 18.5)
- removed the REF** at (226.3, -17.8)
- removed the REF** at (113.8, -54.1)
- removed the REF** at (19.7, 17.3)
- removed the REF** at (96.5, -54.1)
- removed the REF** at (115.6, -33.9)
- removed the REF** at (181.6, -54.7)
- removed the REF** at (264.4, -48.2)
- removed the REF** at (31.0, -48.2)
- removed the REF** at (136.4, -37.5)
- removed STLED1, STLED2: LED_GREEN, LED_SMD:LED_0805_2012Metric
- removed SW1, SW4: BOOT_ALT, Button_Switch_SMD:SW_SPST_PTS810
- removed SW2, SW5: RESET_ALT, Button_Switch_SMD:SW_SPST_PTS810
- removed SW3, SW6: SW_DIP_x04, Button_Switch_SMD:SW_DIP_SPSTx04_Slide_Copal_CHS-04B_W7.62mm_P1.27mm
- removed SW_1: W, locallib:Kailh_socket_ChocV2
- removed SW_10: C, locallib:Kailh_socket_ChocV2
- removed SW_11: V, locallib:Kailh_socket_ChocV2
- removed SW_12: B, locallib:Kailh_socket_ChocV2
- removed SW_13: L_RE, locallib:ChocV2_AND_RotaryEncoder_Alps_EC11E-Switch_Vertical_H20mm_NPTH_MP_minimal
- removed SW_14: LALT, locallib:Kailh_socket_ChocV2
- removed SW_15: LSPC, locallib:Kailh_socket_ChocV2
- removed SW_16: L_CNT, locallib:Kailh_socket_ChocV2
- removed SW_17: I, locallib:Kailh_socket_ChocV2
- removed SW_18: O, locallib:Kailh_socket_ChocV2
- removed SW_19: J, locallib:Kailh_socket_ChocV2
- removed SW_2: E, locallib:Kailh_socket_ChocV2
- removed SW_20: K, locallib:Kailh_socket_ChocV2
- removed SW_21: L, locallib:Kailh_socket_ChocV2
- removed SW_22: -, locallib:Kailh_socket_ChocV2
- removed SW_23: ENT, locallib:Kailh_socket_ChocV2
- removed SW_24: N, locallib:Kailh_socket_ChocV2
- removed SW_25: M, locallib:Kailh_socket_ChocV2
- removed SW_26: <,, locallib:Kailh_socket_ChocV2
- removed SW_27: >., locallib:Kailh_socket_ChocV2
- removed SW_28: ?/, locallib:Kailh_socket_ChocV2
- removed SW_29: R_RE, locallib:ChocV2_AND_RotaryEncoder_Alps_EC11E-Switch_Vertical_H20mm_NPTH_MP_minimal
- removed SW_3: LCTL, locallib:Kailh_socket_ChocV2
- removed SW_30: R_CNT, locallib:Kailh_socket_ChocV2
- removed SW_31: RSPC, locallib:Kailh_socket_ChocV2
- removed SW_32: RALT, locallib:Kailh_socket_ChocV2
- removed SW_33: RWIN, locallib:Kailh_socket_ChocV2
- removed SW_4: A, locallib:Kailh_socket_ChocV2
- removed SW_5: S, locallib:Kailh_socket_ChocV2
- removed SW_6: D, locallib:Kailh_socket_ChocV2
- removed SW_7: F, locallib:Kailh_socket_ChocV2
- removed SW_8: Z, locallib:Kailh_socket_ChocV2
- removed SW_9: X, locallib:Kailh_socket_ChocV2
- removed SW_LWIN1: LWIN, locallib:Kailh_socket_ChocV2
- removed T_L_C0, T_L_C1, T_L_C2, T_L_C3, T_L_C4, T_L_C5, T_L_R0, T_L_R1, T_L_R2, T_L_R3, T_R_C0, T_R_C1, T_R_C2, T_R_C3, T_R_C4, T_R_C5, T_R_R0, T_R_R1, T_R_R2, T_R_R3: Conn_01x01, locallib:TestPoint_THTPad_D2.0mm_Drill1.0mm
- removed U1, U2: NCP1117-3.3_SOT223, Package_TO_SOT_SMD:SOT-223-3_TabPin2
- removed U3, U5: RP2040, locallib:RP2040-QFN-56
- removed U4, U6: W25Q128JVPIQ, Package_SON:WSON-8-1EP_6x5mm_P1.27mm_EP3.4x4.3mm
- removed Y1, Y2: 12MHz, Crystal:Resonator_SMD_Murata_CSTxExxV-3Pin_3.0x1.1mm
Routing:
- net (no net): track 5727.2 -> 0.00 mm, vias 242 -> 0
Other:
- board size 271.5 x 101 mm -> 131 x 83 mm
- board text removed: "#SandyLP_Duo DN0010 by @jpskenn"
- board text removed: "1 2 3 4"
- board text removed: "BOOT"
- board text removed: "L Back"
- board text removed: "Legitimate Anger"
- board text removed: "R Back"
- board text removed: "RESET"
- board text removed: "Through-hole tap head diameter"
- board text removed: "⌨️"
